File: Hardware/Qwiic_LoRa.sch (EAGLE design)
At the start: 37 parts, among them J1 Qwiic Right Angle, J2 Qwiic Right Angle, J4 AVR_SPI_PROG, J5 U.FL, U1 ATMEGA328P_TQFP, U2 RFM96W, Y1 16MHz

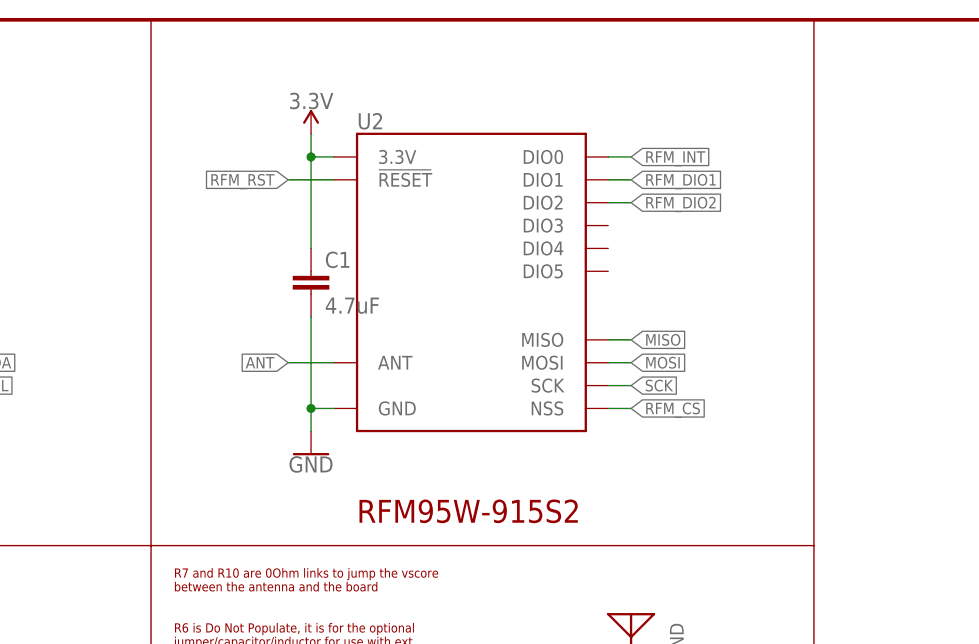
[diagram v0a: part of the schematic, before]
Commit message: Version X03
Add Chip Select pullup on the radio module, only affects programming.
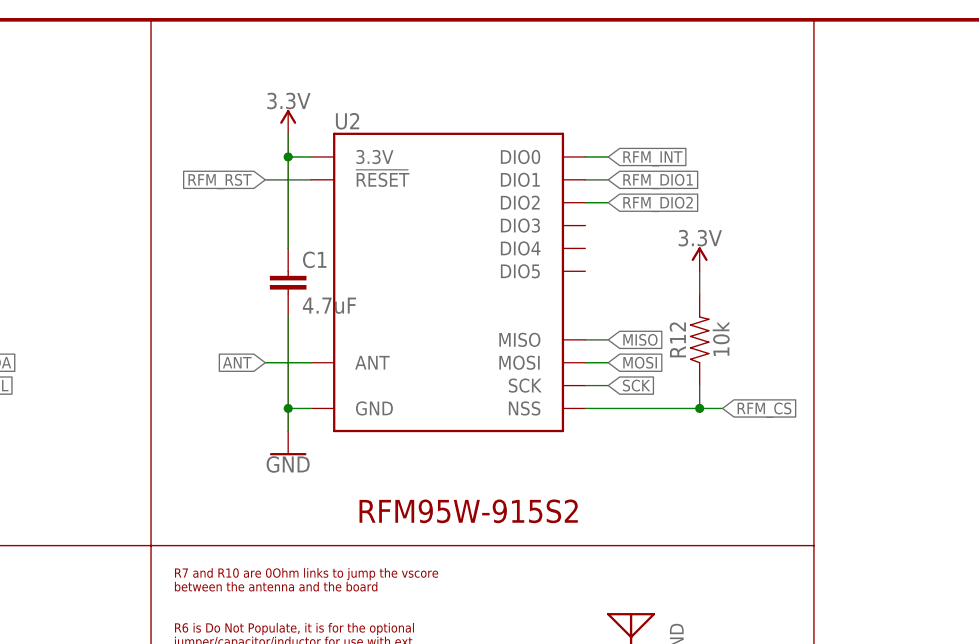
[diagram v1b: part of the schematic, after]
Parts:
- added R12: 10k, SparkFun-Resistors:10KOHM-0603-1/10W-1%
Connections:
- net 3.3V: now also R12.2
- net RFM_CS: now also R12.1
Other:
- moved on the sheet: C1, U2
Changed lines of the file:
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@@
 <part name="TP2" library="SparkFun-Connectors" deviceset="TEST-POINT" device="3" value=""/>
 <part name="TP3" library="SparkFun-Connectors" deviceset="TEST-POINT" device="3" value=""/>
+<part name="R12" library="SparkFun-Resistors" deviceset="10KOHM" device="-0603-1/10W-1%" value="10k"/>
+<part name="SUPPLY4" library="SparkFun-PowerSymbols" deviceset="3.3V" device=""/>
 </parts>
 <sheets>
@@
 <instance part="J1" gate="G$1" x="20.32" y="17.78"/>
 <instance part="J4" gate="G$1" x="27.94" y="53.34"/>
-<instance part="SUPPLY2" gate="G$1" x="73.66" y="172.72"/>
-<instance part="GND2" gate="1" x="73.66" y="137.16"/>
+<instance part="SUPPLY2" gate="G$1" x="71.12" y="172.72"/>
+<instance part="GND2" gate="1" x="71.12" y="137.16"/>
 <instance part="U1" gate="U1" x="190.5" y="121.92"/>
 <instance part="R1" gate="G$1" x="160.02" y="160.02" rot="R90"/>
@@
 <instance part="R9" gate="G$1" x="175.26" y="55.88" rot="R180"/>
 <instance part="GND7" gate="1" x="185.42" y="48.26"/>
-<instance part="U2" gate="G$1" x="91.44" y="154.94"/>
+<instance part="U2" gate="G$1" x="88.9" y="154.94"/>
 <instance part="J6" gate="G$1" x="129.54" y="55.88"/>
-<instance part="C1" gate="G$1" x="73.66" y="154.94"/>
+<instance part="C1" gate="G$1" x="71.12" y="154.94"/>
 <instance part="SUPPLY1" gate="G$1" x="152.4" y="101.6"/>
 <instance part="GND13" gate="1" x="152.4" y="86.36"/>
@@
 <instance part="TP2" gate="G$1" x="76.2" y="55.88" rot="R180"/>
 <instance part="TP3" gate="G$1" x="76.2" y="53.34" rot="R180"/>
+<instance part="R12" gate="G$1" x="116.84" y="149.86" rot="R90"/>
+<instance part="SUPPLY4" gate="G$1" x="116.84" y="157.48"/>
 </instances>
 <busses>
@@
 <net name="3.3V" class="1">
 <segment>
-<wire x1="76.2" y1="170.18" x2="73.66" y2="170.18" width="0.1524" layer="91"/>
-<wire x1="73.66" y1="170.18" x2="73.66" y2="172.72" width="0.1524" layer="91"/>
+<wire x1="73.66" y1="170.18" x2="71.12" y2="170.18" width="0.1524" layer="91"/>
+<wire x1="71.12" y1="170.18" x2="71.12" y2="172.72" width="0.1524" layer="91"/>
 <pinref part="SUPPLY2" gate="G$1" pin="3.3V"/>
 <pinref part="U2" gate="G$1" pin="3.3V"/>
 <pinref part="C1" gate="G$1" pin="1"/>
-<wire x1="73.66" y1="160.02" x2="73.66" y2="170.18" width="0.1524" layer="91"/>
-<junction x="73.66" y="170.18"/>
+<wire x1="71.12" y1="160.02" x2="71.12" y2="170.18" width="0.1524" layer="91"/>
+<junction x="71.12" y="170.18"/>
 </segment>
 <segment>
@@
 <pinref part="C3" gate="G$1" pin="1"/>
 </segment>
+<segment>
+<pinref part="R12" gate="G$1" pin="2"/>
+<wire x1="116.84" y1="154.94" x2="116.84" y2="157.48" width="0.1524" layer="91"/>
+<pinref part="SUPPLY4" gate="G$1" pin="3.3V"/>
+</segment>
 </net>
 <net name="GND" class="0">
 <segment>
-<wire x1="73.66" y1="142.24" x2="73.66" y2="139.7" width="0.1524" layer="91"/>
-<wire x1="76.2" y1="142.24" x2="73.66" y2="142.24" width="0.1524" layer="91"/>
+<wire x1="71.12" y1="142.24" x2="71.12" y2="139.7" width="0.1524" layer="91"/>
+<wire x1="73.66" y1="142.24" x2="71.12" y2="142.24" width="0.1524" layer="91"/>
 <pinref part="GND2" gate="1" pin="GND"/>
 <pinref part="U2" gate="G$1" pin="GND"/>
 <pinref part="C1" gate="G$1" pin="2"/>
-<wire x1="73.66" y1="152.4" x2="73.66" y2="142.24" width="0.1524" layer="91"/>
-<junction x="73.66" y="142.24"/>
+<wire x1="71.12" y1="152.4" x2="71.12" y2="142.24" width="0.1524" layer="91"/>
+<junction x="71.12" y="142.24"/>
 </segment>
 <segment>
@@
 <net name="MISO" class="0">
 <segment>
-<wire x1="106.68" y1="149.86" x2="109.22" y2="149.86" width="0.1524" layer="91"/>
-<label x="109.22" y="149.86" size="1.27" layer="95" xref="yes"/>
+<wire x1="104.14" y1="149.86" x2="106.68" y2="149.86" width="0.1524" layer="91"/>
+<label x="106.68" y="149.86" size="1.27" layer="95" xref="yes"/>
 <pinref part="U2" gate="G$1" pin="MISO"/>
 </segment>
@@
 <net name="MOSI" class="0">
 <segment>
-<wire x1="106.68" y1="147.32" x2="109.22" y2="147.32" width="0.1524" layer="91"/>
-<label x="109.22" y="147.32" size="1.27" layer="95" xref="yes"/>
+<wire x1="104.14" y1="147.32" x2="106.68" y2="147.32" width="0.1524" layer="91"/>
+<label x="106.68" y="147.32" size="1.27" layer="95" xref="yes"/>
 <pinref part="U2" gate="G$1" pin="MOSI"/>
 </segment>
@@
 <net name="SCK" class="0">
 <segment>
-<wire x1="106.68" y1="144.78" x2="109.22" y2="144.78" width="0.1524" layer="91"/>
-<label x="109.22" y="144.78" size="1.27" layer="95" xref="yes"/>
+<wire x1="104.14" y1="144.78" x2="106.68" y2="144.78" width="0.1524" layer="91"/>
+<label x="106.68" y="144.78" size="1.27" layer="95" xref="yes"/>
 <pinref part="U2" gate="G$1" pin="SCK"/>
 </segment>
@@
 <net name="RFM_CS" class="0">
 <segment>
-<wire x1="106.68" y1="142.24" x2="109.22" y2="142.24" width="0.1524" layer="91"/>
-<label x="109.22" y="142.24" size="1.27" layer="95" xref="yes"/>
+<wire x1="104.14" y1="142.24" x2="116.84" y2="142.24" width="0.1524" layer="91"/>
+<label x="119.38" y="142.24" size="1.27" layer="95" xref="yes"/>
 <pinref part="U2" gate="G$1" pin="NSS"/>
+<wire x1="116.84" y1="142.24" x2="119.38" y2="142.24" width="0.1524" layer="91"/>
+<wire x1="116.84" y1="142.24" x2="116.84" y2="144.78" width="0.1524" layer="91"/>
+<junction x="116.84" y="142.24"/>
+<pinref part="R12" gate="G$1" pin="1"/>
 </segment>
 <segment>
@@
 <net name="RFM_RST" class="0">
 <segment>
-<wire x1="76.2" y1="167.64" x2="71.12" y2="167.64" width="0.1524" layer="91"/>
-<label x="71.12" y="167.64" size="1.27" layer="95" rot="R180" xref="yes"/>
+<wire x1="73.66" y1="167.64" x2="68.58" y2="167.64" width="0.1524" layer="91"/>
+<label x="68.58" y="167.64" size="1.27" layer="95" rot="R180" xref="yes"/>
 <pinref part="U2" gate="G$1" pin="!RESET"/>
 </segment>
@@
 <net name="ANT" class="0">
 <segment>
-<wire x1="76.2" y1="147.32" x2="71.12" y2="147.32" width="0.1524" layer="91"/>
-<label x="71.12" y="147.32" size="1.27" layer="95" rot="R180" xref="yes"/>
+<wire x1="73.66" y1="147.32" x2="68.58" y2="147.32" width="0.1524" layer="91"/>
+<label x="68.58" y="147.32" size="1.27" layer="95" rot="R180" xref="yes"/>
 <pinref part="U2" gate="G$1" pin="ANT"/>
 </segment>
@@
 </segment>
 <segment>
-<wire x1="106.68" y1="170.18" x2="109.22" y2="170.18" width="0.1524" layer="91"/>
-<label x="109.22" y="170.18" size="1.27" layer="95" xref="yes"/>
+<wire x1="104.14" y1="170.18" x2="106.68" y2="170.18" width="0.1524" layer="91"/>
+<label x="106.68" y="170.18" size="1.27" layer="95" xref="yes"/>
 <pinref part="U2" gate="G$1" pin="DIO0"/>
 </segment>
@@
 <segment>
 <pinref part="U2" gate="G$1" pin="DIO1"/>
-<wire x1="106.68" y1="167.64" x2="109.22" y2="167.64" width="0.1524" layer="91"/>
-<label x="109.22" y="167.64" size="1.27" layer="95" xref="yes"/>
+<wire x1="104.14" y1="167.64" x2="106.68" y2="167.64" width="0.1524" layer="91"/>
+<label x="106.68" y="167.64" size="1.27" layer="95" xref="yes"/>
 </segment>
 <segment>
@@
 <segment>
 <pinref part="U2" gate="G$1" pin="DIO2"/>
-<wire x1="106.68" y1="165.1" x2="109.22" y2="165.1" width="0.1524" layer="91"/>
-<label x="109.22" y="165.1" size="1.27" layer="95" xref="yes"/>
-</segment>
-<segment>
+<wire x1="104.14" y1="165.1" x2="106.68" y2="165.1" width="0.1524" layer="91"/>
+<label x="106.68" y="165.1" size="1.27" layer="95" xref="yes"/>
+</segment>
+<segment>
